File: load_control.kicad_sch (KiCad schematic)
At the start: 25 parts

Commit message: Fix and tune differential pair and zones
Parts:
- C501, C503, C504: value (none) -> C; footprint (none) -> Capacitor_SMD:C_0805_2012Metric
- C502, C505: value (none) -> 100n; footprint (none) -> Capacitor_SMD:C_0402_1005Metric
- D501: value (none) -> DIODE; footprint (none) -> Diode_SMD:D_0805_2012Metric
- HS501: value (none) -> Heatsink_Pad; footprint (none) -> 0_Heatsink:Heatsink_ASSMANN_WSW_V6560W
- Q501: value (none) -> IPA60R800CE; footprint (none) -> Package_TO_SOT_THT:TO-220-3_Vertical
- Q502, Q503, Q504: value (none) -> Q_NMOS_GSD; footprint (none) -> Package_TO_SOT_SMD:SOT-23
- R501, R502, R503: value (none) -> R_US; footprint (none) -> Resistor_SMD:R_0805_2012Metric
- R504, R505: value (none) -> 10k; footprint (none) -> Resistor_SMD:R_0805_2012Metric
- R506: value (none) -> 5M; footprint (none) -> Resistor_SMD:R_0805_2012Metric
- R507, R508: value (none) -> 50k; footprint (none) -> Resistor_SMD:R_0805_2012Metric
- R509: value (none) -> 100; footprint (none) -> Resistor_SMD:R_0805_2012Metric
- R510: value (none) -> 1; footprint (none) -> Resistor_SMD:R_0805_2012Metric
- R511: value (none) -> 10m; footprint (none) -> Resistor_SMD:R_0805_2012Metric
- TH501: value (none) -> Thermistor_NTC; footprint (none) -> Resistor_SMD:R_0805_2012Metric
- U501, U502: value (none) -> LM358; footprint (none) -> Package_SO:VSSOP-8_3.0x3.0mm_P0.65mm

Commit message: Add partnumbers
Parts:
- C501, C503, C504: value C -> (none); footprint Capacitor_SMD:C_0805_2012Metric -> (none); Manufacturer (none) -> Generic; PartNumber (none) -> Generic
- C502, C505: value 100n -> (none); footprint Capacitor_SMD:C_0402_1005Metric -> (none); Manufacturer (none) -> Generic; PartNumber (none) -> Generic
- D501: value DIODE -> (none); footprint Diode_SMD:D_0805_2012Metric -> (none); Manufacturer (none) -> Micro Commercial Components; PartNumber (none) -> SD101AWS-TP
- HS501: value Heatsink_Pad -> (none); footprint 0_Heatsink:Heatsink_ASSMANN_WSW_V6560W -> (none); Manufacturer (none) -> ASSMANN WSW; PartNumber (none) -> V6560W
- Q501: value IPA60R800CE -> (none); footprint Package_TO_SOT_THT:TO-220-3_Vertical -> (none); Manufacturer (none) -> Infineon; PartNumber (none) -> IPA60R800CE
- Q502, Q503, Q504: value Q_NMOS_GSD -> (none); footprint Package_TO_SOT_SMD:SOT-23 -> (none)
- R501, R502, R503: value R_US -> (none); footprint Resistor_SMD:R_0805_2012Metric -> (none); Manufacturer (none) -> Generic; PartNumber (none) -> Generic
- R504, R505: value 10k -> (none); footprint Resistor_SMD:R_0805_2012Metric -> (none); Manufacturer (none) -> Generic; PartNumber (none) -> Generic
- R506: value 5M -> (none); footprint Resistor_SMD:R_0805_2012Metric -> (none); Manufacturer (none) -> Generic; PartNumber (none) -> Generic
- R507, R508: value 50k -> (none); footprint Resistor_SMD:R_0805_2012Metric -> (none); Manufacturer (none) -> Generic; PartNumber (none) -> Generic
- R509: value 100 -> (none); footprint Resistor_SMD:R_0805_2012Metric -> (none); Manufacturer (none) -> Generic; PartNumber (none) -> Generic
- R510: value 1 -> (none); footprint Resistor_SMD:R_0805_2012Metric -> (none); Manufacturer (none) -> Generic; PartNumber (none) -> Generic
- R511: value 10m -> (none); footprint Resistor_SMD:R_0805_2012Metric -> (none); Manufacturer (none) -> Generic; PartNumber (none) -> Generic
- TH501: value Thermistor_NTC -> (none); footprint Resistor_SMD:R_0805_2012Metric -> (none); Manufacturer (none) -> TDK Corporation; PartNumber (none) -> NTCG103JF103FT1
- U501, U502: value LM358 -> (none); footprint Package_SO:VSSOP-8_3.0x3.0mm_P0.65mm -> (none); PartNumber (none) -> LM358B

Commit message: Fix missing footprints in schematic
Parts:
- C501, C502, C503, C504, C505, R501, R502, R503, R504, R505, R506, R507, R508, R509, R510, R511: now left out of the parts list
- U501, U502: symbol Amplifier_Operational:LM358 -> Amplifier_Operational:LM2904; PartNumber LM358B -> LM2904BAIPWR
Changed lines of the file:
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@@
   )
   (symbol (lib_id "Device:C") (at 46.99 85.09 0) (unit 1)
-    (in_bom yes) (on_board yes) (fields_autoplaced)
+    (in_bom no) (on_board yes) (fields_autoplaced)
     (property "Reference" "C501" (id 0) (at 50.8 83.8199 0)
       (effects (font (size 1.27 1.27)) (justify left))
@@
   )
   (symbol (lib_id "Device:R_US") (at 151.13 106.68 180) (unit 1)
-    (in_bom yes) (on_board yes) (fields_autoplaced)
+    (in_bom no) (on_board yes) (fields_autoplaced)
     (property "Reference" "R509" (id 0) (at 153.67 105.4099 0)
       (effects (font (size 1.27 1.27)) (justify right))
@@
     (pin "1")
   )
-  (symbol (lib_id "Amplifier_Operational:LM358") (at 153.67 48.26 0) (unit 1)
+  (symbol (lib_id "Amplifier_Operational:LM2904") (at 153.67 48.26 0) (unit 1)
     (in_bom yes) (on_board yes) (fields_autoplaced)
     (property "Reference" "U502" (id 0) (at 153.67 38.1 0))
@@
       (effects (font (size 1.27 1.27)) hide)
     )
-    (property "Datasheet" "http://www.ti.com/lit/ds/symlink/lm2904-n.pdf" (id 3) (at 153.67 48.26 0)
+    (property "Datasheet" "http://www.ti.com/lit/ds/symlink/lm358.pdf" (id 3) (at 153.67 48.26 0)
       (effects (font (size 1.27 1.27)) hide)
     )
@@
       (effects (font (size 1.27 1.27)) hide)
     )
-    (property "PartNumber" "LM358B" (id 5) (at 153.67 48.26 0)
+    (property "PartNumber" "LM2904BAIPWR" (id 5) (at 153.67 48.26 0)
       (effects (font (size 1.27 1.27)) hide)
     )
@@
   )
   (symbol (lib_id "Device:R_US") (at 137.16 72.39 90) (mirror x) (unit 1)
-    (in_bom yes) (on_board yes)
+    (in_bom no) (on_board yes)
     (property "Reference" "R508" (id 0) (at 138.4301 69.85 0)
       (effects (font (size 1.27 1.27)) (justify right))
@@
   )
   (symbol (lib_id "Device:C") (at 68.58 127 270) (unit 1)
-    (in_bom yes) (on_board yes)
+    (in_bom no) (on_board yes)
     (property "Reference" "C503" (id 0) (at 60.96 125.73 90))
     (property "Value" "" (id 1) (at 73.66 125.73 90))
@@
   )
   (symbol (lib_id "Device:R_US") (at 36.83 81.28 90) (unit 1)
-    (in_bom yes) (on_board yes)
+    (in_bom no) (on_board yes)
     (property "Reference" "R501" (id 0) (at 36.83 78.74 90))
     (property "Value" "" (id 1) (at 36.83 85.09 90))
@@
     (pin "2")
   )
-  (symbol (lib_id "Amplifier_Operational:LM358") (at 66.04 48.26 90) (unit 3)
+  (symbol (lib_id "Amplifier_Operational:LM2904") (at 66.04 48.26 90) (unit 3)
     (in_bom yes) (on_board yes) (fields_autoplaced)
     (property "Reference" "U501" (id 0) (at 66.04 45.72 90))
@@
       (effects (font (size 1.27 1.27)) hide)
     )
-    (property "Datasheet" "http://www.ti.com/lit/ds/symlink/lm2904-n.pdf" (id 3) (at 66.04 48.26 0)
+    (property "Datasheet" "http://www.ti.com/lit/ds/symlink/lm358.pdf" (id 3) (at 66.04 48.26 0)
       (effects (font (size 1.27 1.27)) hide)
     )
@@
       (effects (font (size 1.27 1.27)) hide)
     )
-    (property "PartNumber" "LM358B" (id 5) (at 66.04 48.26 0)
+    (property "PartNumber" "LM2904BAIPWR" (id 5) (at 66.04 48.26 0)
       (effects (font (size 1.27 1.27)) hide)
     )
@@
   )
   (symbol (lib_id "Device:R_US") (at 78.74 134.62 0) (unit 1)
-    (in_bom yes) (on_board yes)
+    (in_bom no) (on_board yes)
     (property "Reference" "R503" (id 0) (at 81.28 133.35 0)
       (effects (font (size 1.27 1.27)) (justify left))
@@
   )
   (symbol (lib_id "Device:R_US") (at 97.79 87.63 180) (unit 1)
-    (in_bom yes) (on_board yes)
+    (in_bom no) (on_board yes)
     (property "Reference" "R504" (id 0) (at 100.33 86.3599 0)
       (effects (font (size 1.27 1.27)) (justify right))
@@
     (pin "1")
   )
-  (symbol (lib_id "Amplifier_Operational:LM358") (at 195.58 20.32 90) (unit 3)
+  (symbol (lib_id "Amplifier_Operational:LM2904") (at 195.58 20.32 90) (unit 3)
     (in_bom yes) (on_board yes) (fields_autoplaced)
     (property "Reference" "U502" (id 0) (at 195.58 17.78 90))
@@
       (effects (font (size 1.27 1.27)) hide)
     )
-    (property "Datasheet" "http://www.ti.com/lit/ds/symlink/lm2904-n.pdf" (id 3) (at 195.58 20.32 0)
+    (property "Datasheet" "http://www.ti.com/lit/ds/symlink/lm358.pdf" (id 3) (at 195.58 20.32 0)
       (effects (font (size 1.27 1.27)) hide)
     )
@@
       (effects (font (size 1.27 1.27)) hide)
     )
-    (property "PartNumber" "LM358B" (id 5) (at 195.58 20.32 0)
+    (property "PartNumber" "LM2904BAIPWR" (id 5) (at 195.58 20.32 0)
       (effects (font (size 1.27 1.27)) hide)
     )
@@
   )
   (symbol (lib_id "Device:R_US") (at 227.33 106.68 180) (unit 1)
-    (in_bom yes) (on_board yes) (fields_autoplaced)
+    (in_bom no) (on_board yes) (fields_autoplaced)
     (property "Reference" "R511" (id 0) (at 229.87 105.4099 0)
       (effects (font (size 1.27 1.27)) (justify right))
@@
   )
   (symbol (lib_id "Device:R_US") (at 113.03 106.68 180) (unit 1)
-    (in_bom yes) (on_board yes)
+    (in_bom no) (on_board yes)
     (property "Reference" "R505" (id 0) (at 115.57 105.4099 0)
       (effects (font (size 1.27 1.27)) (justify right))
@@
     (pin "2")
   )
-  (symbol (lib_id "Amplifier_Operational:LM358") (at 67.31 83.82 0) (unit 2)
+  (symbol (lib_id "Amplifier_Operational:LM2904") (at 67.31 83.82 0) (unit 2)
     (in_bom yes) (on_board yes) (fields_autoplaced)
     (property "Reference" "U501" (id 0) (at 67.31 73.66 0))
@@
       (effects (font (size 1.27 1.27)) hide)
     )
-    (property "Datasheet" "http://www.ti.com/lit/ds/symlink/lm2904-n.pdf" (id 3) (at 67.31 83.82 0)
+    (property "Datasheet" "http://www.ti.com/lit/ds/symlink/lm358.pdf" (id 3) (at 67.31 83.82 0)
       (effects (font (size 1.27 1.27)) hide)
     )
@@
       (effects (font (size 1.27 1.27)) hide)
     )
-    (property "PartNumber" "LM358B" (id 5) (at 67.31 83.82 0)
+    (property "PartNumber" "LM2904BAIPWR" (id 5) (at 67.31 83.82 0)
       (effects (font (size 1.27 1.27)) hide)
     )
@@
     (pin "8")
   )
-  (symbol (lib_id "Amplifier_Operational:LM358") (at 67.31 102.87 0) (mirror y) (unit 1)
+  (symbol (lib_id "Amplifier_Operational:LM2904") (at 67.31 102.87 0) (mirror y) (unit 1)
     (in_bom yes) (on_board yes) (fields_autoplaced)
     (property "Reference" "U501" (id 0) (at 67.31 92.71 0))
@@
       (effects (font (size 1.27 1.27)) hide)
     )
-    (property "Datasheet" "http://www.ti.com/lit/ds/symlink/lm2904-n.pdf" (id 3) (at 67.31 102.87 0)
+    (property "Datasheet" "http://www.ti.com/lit/ds/symlink/lm358.pdf" (id 3) (at 67.31 102.87 0)
       (effects (font (size 1.27 1.27)) hide)
     )
@@
       (effects (font (size 1.27 1.27)) hide)
     )
-    (property "PartNumber" "LM358B" (id 5) (at 67.31 102.87 0)
+    (property "PartNumber" "LM2904BAIPWR" (id 5) (at 67.31 102.87 0)
       (effects (font (size 1.27 1.27)) hide)
     )
@@
   )
   (symbol (lib_id "Device:R_US") (at 189.23 106.68 180) (unit 1)
-    (in_bom yes) (on_board yes) (fields_autoplaced)
+    (in_bom no) (on_board yes) (fields_autoplaced)
     (property "Reference" "R510" (id 0) (at 191.77 105.4099 0)
       (effects (font (size 1.27 1.27)) (justify right))
@@
   )
   (symbol (lib_id "Device:C") (at 101.6 106.68 180) (unit 1)
-    (in_bom yes) (on_board yes) (fields_autoplaced)
+    (in_bom no) (on_board yes) (fields_autoplaced)
     (property "Reference" "C504" (id 0) (at 105.41 105.4099 0)
       (effects (font (size 1.27 1.27)) (justify right))
@@
   )
   (symbol (lib_id "Device:C_Small") (at 184.15 27.94 0) (unit 1)
-    (in_bom yes) (on_board yes) (fields_autoplaced)
+    (in_bom no) (on_board yes) (fields_autoplaced)
     (property "Reference" "C505" (id 0) (at 186.69 26.6762 0)
       (effects (font (size 1.27 1.27)) (justify left))
@@
   )
   (symbol (lib_id "Device:R_US") (at 134.62 52.07 0) (mirror y) (unit 1)
-    (in_bom yes) (on_board yes)
+    (in_bom no) (on_board yes)
     (property "Reference" "R507" (id 0) (at 137.16 53.3401 0)
       (effects (font (size 1.27 1.27)) (justify right))
@@
   )
   (symbol (lib_id "Device:C_Small") (at 54.61 55.88 0) (unit 1)
-    (in_bom yes) (on_board yes) (fields_autoplaced)
+    (in_bom no) (on_board yes) (fields_autoplaced)
     (property "Reference" "C502" (id 0) (at 57.15 54.6162 0)
       (effects (font (size 1.27 1.27)) (justify left))
@@
   )
   (symbol (lib_id "Device:R_US") (at 127 45.72 90) (unit 1)
-    (in_bom yes) (on_board yes)
+    (in_bom no) (on_board yes)
     (property "Reference" "R506" (id 0) (at 128.2701 48.26 0)
       (effects (font (size 1.27 1.27)) (justify right))
@@
     (pin "2")
   )
-  (symbol (lib_id "Amplifier_Operational:LM358") (at 168.91 74.93 0) (unit 2)
+  (symbol (lib_id "Amplifier_Operational:LM2904") (at 168.91 74.93 0) (unit 2)
     (in_bom yes) (on_board yes)
     (property "Reference" "U502" (id 0) (at 168.91 64.77 0))
@@
       (effects (font (size 1.27 1.27)) hide)
     )
-    (property "Datasheet" "http://www.ti.com/lit/ds/symlink/lm2904-n.pdf" (id 3) (at 168.91 74.93 0)
+    (property "Datasheet" "http://www.ti.com/lit/ds/symlink/lm358.pdf" (id 3) (at 168.91 74.93 0)
       (effects (font (size 1.27 1.27)) hide)
     )
@@
       (effects (font (size 1.27 1.27)) hide)
     )
-    (property "PartNumber" "LM358B" (id 5) (at 168.91 74.93 0)
+    (property "PartNumber" "LM2904BAIPWR" (id 5) (at 168.91 74.93 0)
       (effects (font (size 1.27 1.27)) hide)
     )
@@
   )
   (symbol (lib_id "Device:R_US") (at 68.58 115.57 270) (unit 1)
-    (in_bom yes) (on_board yes)
+    (in_bom no) (on_board yes)
     (property "Reference" "R502" (id 0) (at 62.23 114.3 90))
     (property "Value" "" (id 1) (at 73.66 114.3 90))

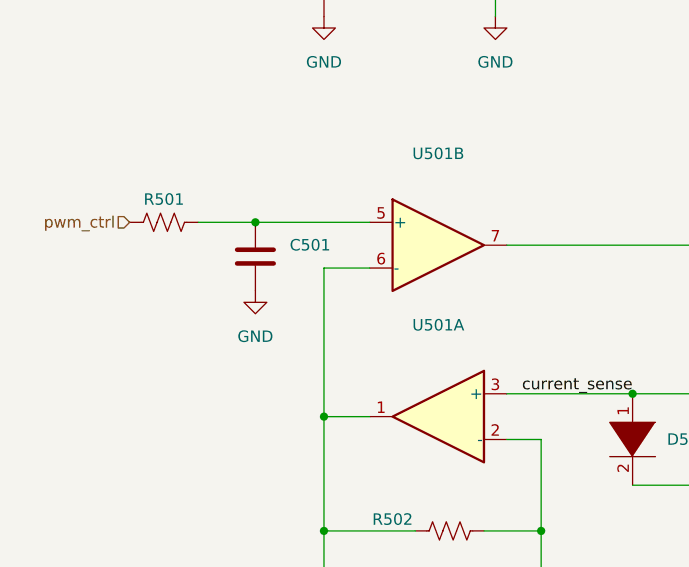
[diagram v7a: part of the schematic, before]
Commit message: Change some partnumbers in preparation for the order
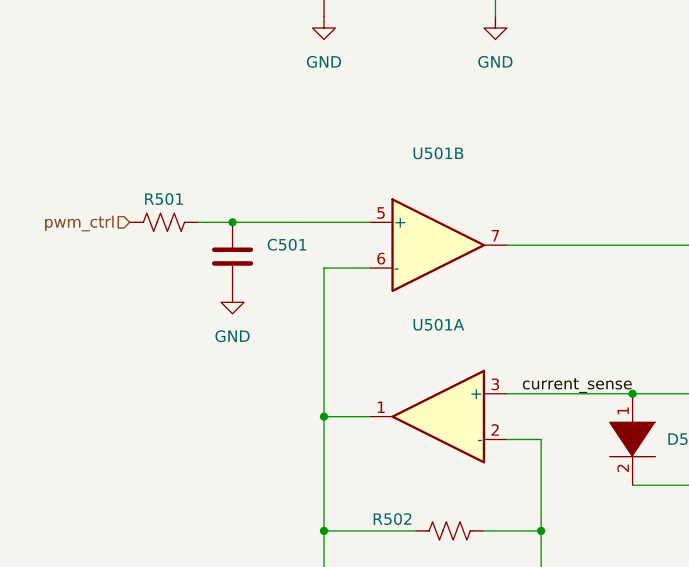
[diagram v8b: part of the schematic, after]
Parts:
- Q501: Manufacturer Infineon -> On Semiconductor; PartNumber IPA60R800CE -> IRLS640A
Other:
- moved on the sheet: C501
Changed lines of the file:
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@@
   (junction (at 78.74 127) (diameter 0) (color 0 0 0 0)
   )
-  (junction (at 46.99 81.28) (diameter 0) (color 0 0 0 0)
-  )
   (junction (at 54.61 102.87) (diameter 0) (color 0 0 0 0)
   )
@@
   )
   (junction (at 101.6 110.49) (diameter 0) (color 0 0 0 0)
+  )
+  (junction (at 44.45 81.28) (diameter 0) (color 0 0 0 0)
   )
   (junction (at 54.61 115.57) (diameter 0) (color 0 0 0 0)
@@
     (stroke (width 0) (type default) (color 0 0 0 0))
   )
-  (wire (pts (xy 46.99 81.28) (xy 59.69 81.28))
-    (stroke (width 0) (type default) (color 0 0 0 0))
-  )
   (wire (pts (xy 180.34 96.52) (xy 181.61 96.52))
     (stroke (width 0) (type default) (color 0 0 0 0))
@@
     (stroke (width 0) (type default) (color 0 0 0 0))
   )
+  (wire (pts (xy 44.45 81.28) (xy 59.69 81.28))
+    (stroke (width 0) (type default) (color 0 0 0 0))
+  )
   (wire (pts (xy 54.61 115.57) (xy 64.77 115.57))
     (stroke (width 0) (type default) (color 0 0 0 0))
@@
     (stroke (width 0) (type default) (color 0 0 0 0))
   )
-  (wire (pts (xy 40.64 81.28) (xy 46.99 81.28))
+  (wire (pts (xy 40.64 81.28) (xy 44.45 81.28))
     (stroke (width 0) (type default) (color 0 0 0 0))
   )
@@
     (effects (font (size 1.27 1.27)) (justify left))
   )
-  (symbol (lib_id "Device:C") (at 46.99 85.09 0) (unit 1)
+  (symbol (lib_id "Device:C") (at 44.45 85.09 0) (unit 1)
     (in_bom no) (on_board yes) (fields_autoplaced)
-    (property "Reference" "C501" (id 0) (at 50.8 83.8199 0)
-      (effects (font (size 1.27 1.27)) (justify left))
-    )
-    (property "Value" "" (id 1) (at 50.8 86.3599 0)
-      (effects (font (size 1.27 1.27)) (justify left))
-    )
-    (property "Footprint" "" (id 2) (at 47.9552 88.9 0)
-      (effects (font (size 1.27 1.27)) hide)
-    )
-    (property "Datasheet" "~" (id 3) (at 46.99 85.09 0)
-      (effects (font (size 1.27 1.27)) hide)
-    )
-    (property "Manufacturer" "Generic" (id 4) (at 46.99 85.09 0)
-      (effects (font (size 1.27 1.27)) hide)
-    )
-    (property "PartNumber" "Generic" (id 5) (at 46.99 85.09 0)
+    (property "Reference" "C501" (id 0) (at 48.26 83.8199 0)
+      (effects (font (size 1.27 1.27)) (justify left))
+    )
+    (property "Value" "" (id 1) (at 48.26 86.3599 0)
+      (effects (font (size 1.27 1.27)) (justify left))
+    )
+    (property "Footprint" "" (id 2) (at 45.4152 88.9 0)
+      (effects (font (size 1.27 1.27)) hide)
+    )
+    (property "Datasheet" "~" (id 3) (at 44.45 85.09 0)
+      (effects (font (size 1.27 1.27)) hide)
+    )
+    (property "Manufacturer" "Generic" (id 4) (at 44.45 85.09 0)
+      (effects (font (size 1.27 1.27)) hide)
+    )
+    (property "PartNumber" "Generic" (id 5) (at 44.45 85.09 0)
       (effects (font (size 1.27 1.27)) hide)
     )
@@
       (effects (font (size 1.27 1.27)) hide)
     )
-    (property "Manufacturer" "Infineon" (id 4) (at 110.49 83.82 0)
-      (effects (font (size 1.27 1.27)) hide)
-    )
-    (property "PartNumber" "IPA60R800CE" (id 5) (at 110.49 83.82 0)
+    (property "Manufacturer" "On Semiconductor" (id 4) (at 110.49 83.82 0)
+      (effects (font (size 1.27 1.27)) hide)
+    )
+    (property "PartNumber" "IRLS640A" (id 5) (at 110.49 83.82 0)
       (effects (font (size 1.27 1.27)) hide)
     )
@@
     (pin "1")
   )
-  (symbol (lib_id "power:GND") (at 46.99 88.9 0) (unit 1)
-    (in_bom yes) (on_board yes) (fields_autoplaced)
-    (property "Reference" "#PWR0501" (id 0) (at 46.99 95.25 0)
-      (effects (font (size 1.27 1.27)) hide)
-    )
-    (property "Value" "GND" (id 1) (at 46.99 93.98 0))
-    (property "Footprint" "" (id 2) (at 46.99 88.9 0)
-      (effects (font (size 1.27 1.27)) hide)
-    )
-    (property "Datasheet" "" (id 3) (at 46.99 88.9 0)
-      (effects (font (size 1.27 1.27)) hide)
-    )
+  (symbol (lib_id "power:GND") (at 44.45 88.9 0) (unit 1)
+    (in_bom yes) (on_board yes) (fields_autoplaced)
+    (property "Reference" "#PWR0501" (id 0) (at 44.45 95.25 0)
+      (effects (font (size 1.27 1.27)) hide)
+    )
+    (property "Value" "GND" (id 1) (at 44.45 93.98 0))
+    (property "Footprint" "" (id 2) (at 44.45 88.9 0)
+      (effects (font (size 1.27 1.27)) hide)
+    )
+    (property "Datasheet" "" (id 3) (at 44.45 88.9 0)
+      (effects (font (size 1.27 1.27)) hide)
+    )
